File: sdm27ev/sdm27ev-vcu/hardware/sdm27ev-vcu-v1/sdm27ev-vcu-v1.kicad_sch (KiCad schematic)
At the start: 33 parts, among them J1 6437288-1, J2 6437288-1, J4 2201778-1, SW2 SW_Push, SW3 SW_Push, U1 ESP32-P4-Core

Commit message: notes from ev vcu design review 10 3
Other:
- note added: "add sdmmc pullups"
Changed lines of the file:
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@@
+		)
+	)
+	(text "add sdmmc pullups\n"
+		(exclude_from_sim no)
+		(at 96.52 59.436 0)
+		(effects
+			(font
+				(size 1.27 1.27)
+			)
 		)
 	)

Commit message: VCU updates
Updated P4 Symbol
Digital IO protection rework done
Added pending fixes from design review, e.x SDMC pullups
Needs power review - add this to ToDo
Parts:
- removed C1, C2, C3, C5, C6: 100nF, Capacitor_SMD:C_0603_1608Metric, symbol Device:C_Small
- removed C4: 10uF, Capacitor_SMD:C_0603_1608Metric, symbol Device:C_Small
- removed R1, R2: 10k, Resistor_SMD:R_0603_1608Metric, symbol Device:R_Small
- removed SW3: SW_Push, Button_Switch_SMD:SW_SPST_CK_KXT3, symbol Switch:SW_Push
- removed U1: ESP32-P4-Core, symbol SDM_EV:ESP32-P4-Core
- added C10: 10uF, Capacitor_SMD:C_0603_1608Metric, symbol Device:C_Small
- added C11: 100nF, Capacitor_SMD:C_0603_1608Metric, symbol Device:C_Small
- added R80: 10k, Resistor_SMD:R_0603_1608Metric, symbol Device:R_Small
- added RN5: 10k, Resistor_SMD:R_Array_Convex_4x0603, symbol Device:R_Pack04
- added SW1: SW_Push, Button_Switch_SMD:SW_SPST_CK_KXT3, symbol Switch:SW_Push
- added U1: WT0132P4-A1, symbol SDM_EV:WT0132P4-A1
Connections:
- net P4_Reset is gone; now on an unnamed net: R9.1
- net 3.3V: now also R104.2, R87.2; no longer R104.1, R87.1
- net A1: now also U1.74 (GPIO16)
- net A2: now also U1.75 (GPIO17)
- net A3: now also U1.76 (GPIO18)
- net A4: now also U1.77 (GPIO19)
- net A5: now also U1.48 (GPIO49)
- net A6: now also U1.49 (GPIO50)
- net A7: now also U1.50 (GPIO51)
- net A8: now also U1.51 (GPIO52)
- net CAN1_TERM: now also U1.71 (GPIO0)
- net CAN2_TERM: now also U1.72 (GPIO1)
- net CAN3_RX: now also U1.65 (GPIO11)
- net CAN3_TERM: now also U1.55 (GPIO2)
- net CAN3_TX: now also U1.63 (GPIO10)
- net CAN_INT_1: now also U1.61 (GPIO8)
- net CAN_INT_2: now also U1.62 (GPIO9)
- net CAN_SPI2_CS1: now also U1.56 (GPIO3)
- net CAN_SPI2_CS2: now also U1.57 (GPIO4)
- net CAN_SPI2_SCK: now also U1.59 (GPIO6)
- net CAN_SPI2_SDI: now also U1.60 (GPIO7)
- net CAN_SPI2_SDO: now also U1.58 (GPIO5)
- net DI1: now also U1.66 (GPIO12)
- net DI2: now also U1.67 (GPIO13)
- net DI3: now also U1.68 (GPIO14)
- net DI4: now also U1.69 (GPIO15)
- net DO1: now also U1.19 (GPIO24)
- net DO2: now also U1.20 (GPIO25)
- net DO3: now also U1.22 (GPIO26)
- net DO4: now also U1.23 (GPIO27)
- net DO5: now also U1.24 (GPIO28)
- net DO6: now also U1.25 (GPIO29)
- net DO7: now also U1.26 (GPIO30)
- net DO8: now also U1.27 (GPIO31)
- net GND: now also SW2.2, C10.2, C11.2, SW1.1, U1.1 (GND), U1.15 (GND), U1.18 (GND), U1.21 (GND), U1.42 (GND), U1.53 (GND), U1.64 (GND), U1.73 (GND), U1.8 (GND), U1.82 (GND); no longer SW2.1
- net PWR_SCL: now also R87.1; no longer R87.2
- net PWR_SDA: now also R104.1; no longer R104.2
- net SD1-CLK: now also U1.40 (GPIO43)
- net SD1-CMD: now also R80.1, U1.43 (GPIO44)
- net SD1-DAT0: now also RN5.4 (R4.1), U1.36 (GPIO39)
- net SD1-DAT1: now also RN5.3 (R3.1), U1.37 (GPIO40)
- net SD1-DAT2: now also RN5.2 (R2.1), U1.38 (GPIO41)
- net SD1-DAT3: now also RN5.1 (R1.1), U1.39 (GPIO42)
- net StatLED1: now also U1.28 (GPIO32)
- net StatLED2: now also U1.29 (GPIO33)
- net at R51.2: now also U1.16 (USB_DM)
- net at R7.1: now also U1.33 (GPIO36)
- net at R50.1: now also U1.17 (USB_DP)
- net P4_Boot: no longer names the net of R8.1
- net P4_Boot: now also SW2.1, SW1.2, U1.31 (GPIO35), U1.70 (CHIP_PU); no longer SW2.2
- new net 5V: C10.1, C11.1, U1.41 (VCC)
- new net ESP_LDO: R80.2, RN5.5 (R4.2), RN5.6 (R3.2), RN5.7 (R2.2), RN5.8 (R1.2), U1.32 (ESP_LDO_VO4)
- no-connect marks 20 -> 28
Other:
- sheet Digital IO renamed Digital IN-OUT
- sheet Analog ports: added none; removed 5VA, A1_5V, A1_CONN, A2_5V, A2_CONN, A3_5V, A3_CONN, A4_5V, A4_CONN, A5_5V, A5_CONN, A6_5V, A6_CONN, A7_5V, A7_CONN, A8_5V, A8_CONN, A_PWR_INT, SCL, SDA
- sheet CAN ports: added none; removed CAN3_STB, CAN4+, CAN4-, CAN4_RX, CAN4_STB, CAN4_TERM, CAN4_TX, CAN_SPI2_CS2
- sheet Digital IN-OUT ports: added none; removed DI1_CONN, DI2_CONN, DI3_CONN, DI4_CONN, DO1_CONN, DO2_CONN, DO3_CONN, DO4_CONN, DO5_CONN, DO6_CONN, DO7_CONN, DO8_CONN
- note added: "needs power change*"
- note removed: "BULK"
- note removed: "HW SPI*"
- note removed: "add sdmmc pullups"
- moved on the sheet: LED1, LED2, LED3, R106, R107, R108, R14, R15

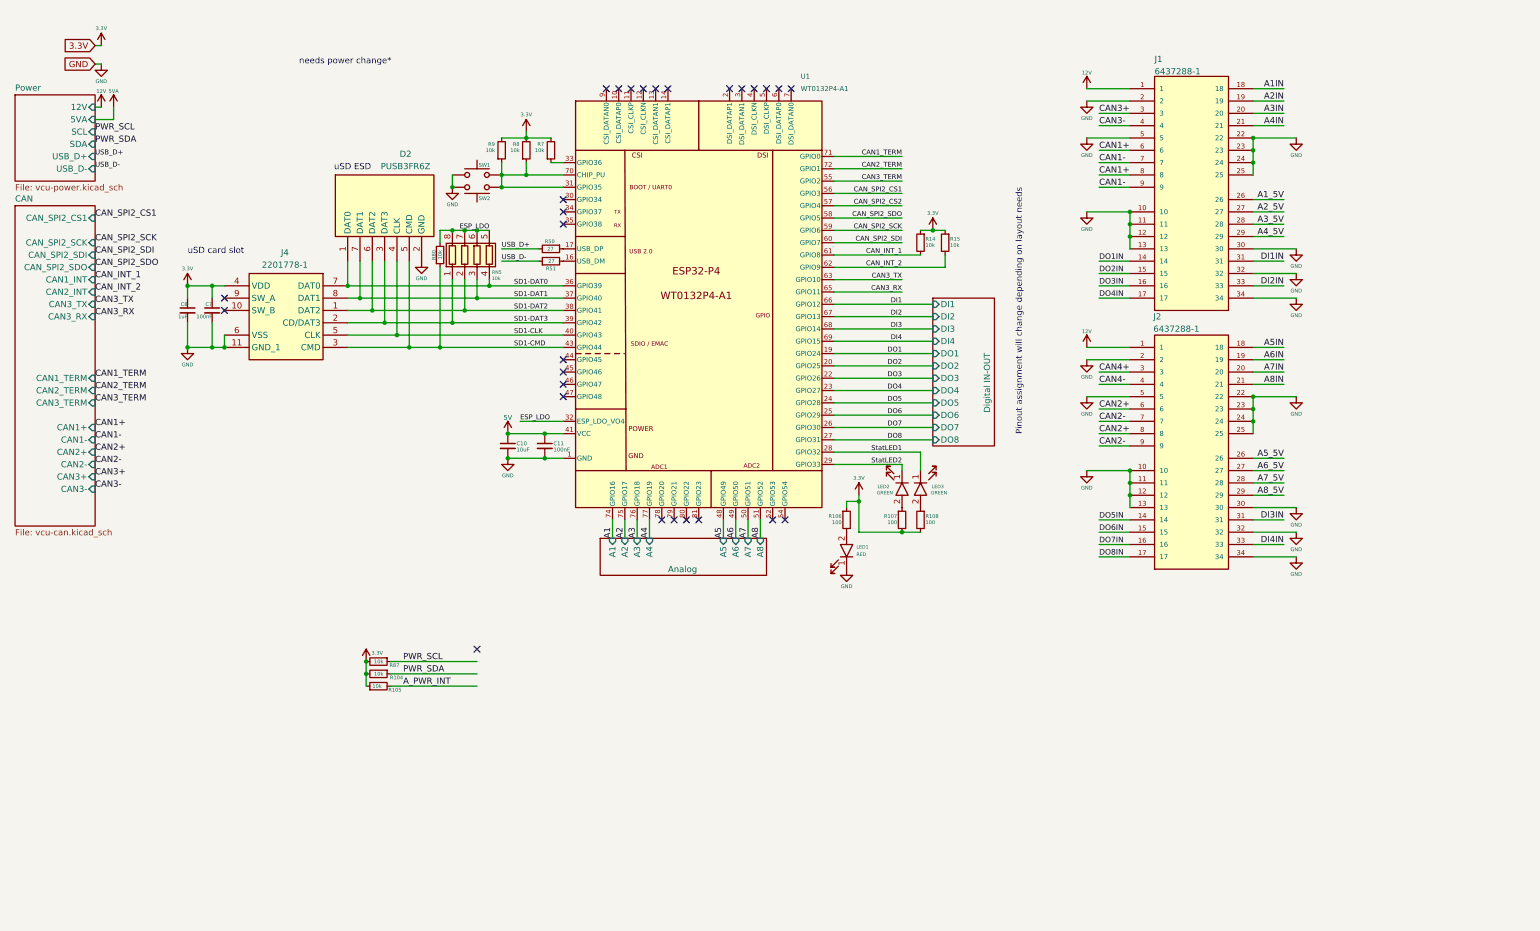
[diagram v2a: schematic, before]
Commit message: VCU sch reorg and power rework
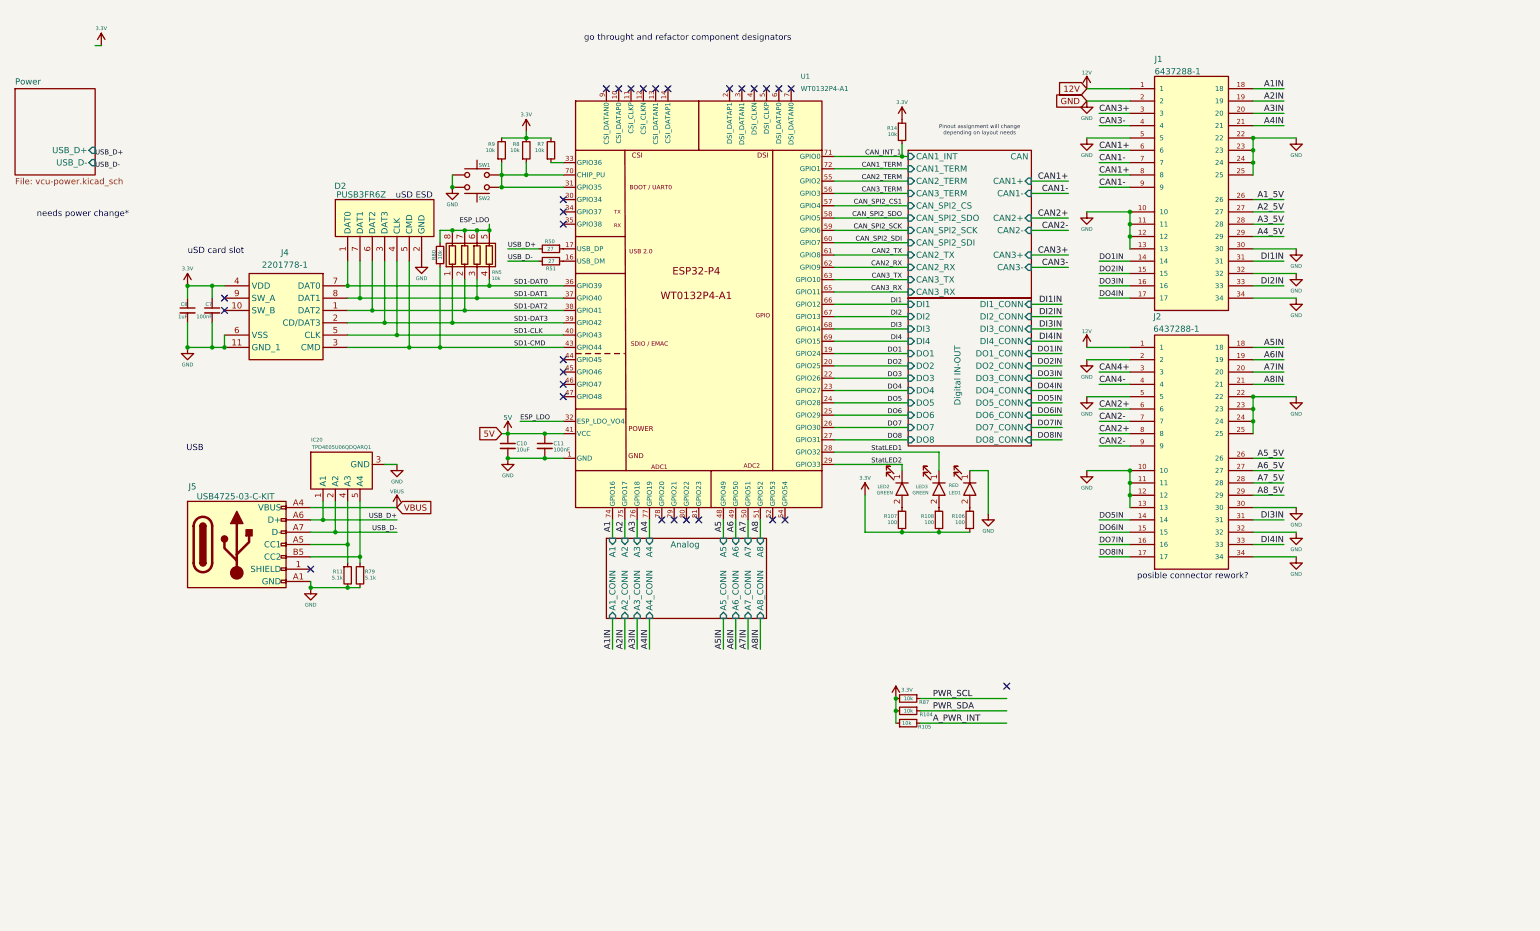
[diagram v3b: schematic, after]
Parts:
- removed R15: 10k, Resistor_SMD:R_0603_1608Metric, symbol Device:R_Small
- added IC20: TPD4E05U06QDQARQ1, DQA(R-PUSON-N10), symbol SDM_EV:TPD4E05U06QDQARQ1
- added J5: USB4725-03-C-KIT, SDM_Misc:GCT_USB4730-GF-A_REVA, symbol SDM_MISC:USB4725-03-C-KIT
- added R11, R79: 5.1k, Resistor_SMD:R_0603_1608Metric, symbol Device:R_Small
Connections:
- net CAN_SPI2_CS2 is gone; now on net CAN_SPI2_CS1: U1.57 (GPIO4)
- net CAN1_TERM: now also U1.72 (GPIO1); no longer U1.71 (GPIO0)
- net CAN2_TERM: now also U1.55 (GPIO2); no longer U1.72 (GPIO1)
- net CAN3_TERM: now also U1.56 (GPIO3); no longer U1.55 (GPIO2)
- net CAN_INT_1: now also U1.71 (GPIO0); no longer U1.61 (GPIO8)
- net CAN_SPI2_CS1: no longer U1.56 (GPIO3)
- net GND: now also IC20.3 (GND), IC20.8 (GND_2), J5.A1 (GND), R11.2, R79.2
- net USB_D+: now also IC20.1 (A1), J5.A6 (D+), J5.B6 (D+)
- net USB_D-: now also IC20.2 (A2), J5.A7 (D-), J5.B7 (D-)
- net CAN_INT_2 renamed CAN2_RX
- new net: IC20.5 (A4), J5.B5 (CC2), R79.1
- new net: IC20.4 (A3), J5.A5 (CC1), R11.1
- new net: IC20.10 (NC_3), IC20.6 (NC_4), IC20.7 (NC_1), IC20.9 (NC_2)
- new net CAN2_TX: U1.61 (GPIO8)
- new net VBUS: J5.A4 (VBUS)
- no-connect marks 28 -> 29
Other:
- sheet Analog ports: added A1_CONN, A2_CONN, A3_CONN, A4_CONN, A5_CONN, A6_CONN, A7_CONN, A8_CONN; removed none
- sheet CAN ports: added CAN2_RX, CAN2_TX, CAN_SPI2_CS; removed CAN2_INT, CAN_SPI2_CS1
- sheet Digital IN-OUT ports: added DI1_CONN, DI2_CONN, DI3_CONN, DI4_CONN, DO1_CONN, DO2_CONN, DO3_CONN, DO4_CONN, DO5_CONN, DO6_CONN, DO7_CONN, DO8_CONN; removed none
- sheet Power ports: added none; removed 12V, 5VA, SCL, SDA
- note added: "USB"
- note added: "go throught and refactor component designators"
- note added: "posible connector rework?"
- moved on the sheet: D2, LED3, R104, R105, R108, R87

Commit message: EV VCU edits, mostly organizational and pre layout/footprint assigned
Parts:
- removed J1, J2: 6437288-1, SDM27 EV VCU:TE_6437288-1, symbol EV VCU:6437288-1
- added J1, J2: 1-776087-1, SDM_EV:17760871, symbol SDM_EV:1-776087-1
- added J3, J6: 6437288-4, SDM_EV:64372884, symbol SDM_EV:6437288-4
- D2: footprint PUSB3FR6Z -> (none)
- IC20: footprint DQA(R-PUSON-N10) -> (none)
- J4: footprint 22017781 -> SDM_EV:22017781
- R50, R51: footprint Resistor_SMD:R_0402_1005Metric -> Resistor_SMD:R_0603_1608Metric
- U1: footprint (none) -> SDM_EV:WT0132P4-A1
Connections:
- net 12V: now also J2.1
- net A1IN: now also J1.1, J3.1
- net A1_5V: now also J1.18, J3.8
- net A2IN: now also J1.2, J3.2
- net A2_5V: now also J1.22, J3.10
- net A3IN: now also J1.3, J3.3
- net A3_5V: now also J2.18
- net A4IN: now also J1.4, J3.4
- net A4_5V: now also J2.22
- net A5IN: now also J2.16
- net A6IN: now also J2.17
- net A7IN: now also J2.20
- net A8IN: now also J2.21
- net CAN1+: now also J2.3
- net CAN1-: now also J2.4
- net CAN2+: now also J1.15
- net CAN2-: now also J1.14
- net CAN2_RX: now also U1.52 (GPIO53); no longer U1.62 (GPIO9)
- net CAN2_TX: now also U1.54 (GPIO54); no longer U1.61 (GPIO8)
- net CAN3+: now also J2.6
- net CAN3-: now also J2.7
- net DI1: now also U1.69 (GPIO15); no longer U1.66 (GPIO12)
- net DI2: now also U1.68 (GPIO14); no longer U1.67 (GPIO13)
- net DI3: now also U1.66 (GPIO12); no longer U1.68 (GPIO14)
- net DI3IN: now also J2.14
- net DI4: now also U1.67 (GPIO13); no longer U1.69 (GPIO15)
- net DI4IN: now also J2.15
- net DO1: now also U1.44 (GPIO45); no longer U1.19 (GPIO24)
- net DO1IN: now also J1.5, J3.12
- net DO2: now also U1.45 (GPIO46); no longer U1.20 (GPIO25)
- net DO2IN: now also J1.6, J3.6
- net DO3: now also U1.46 (GPIO47); no longer U1.22 (GPIO26)
- net DO3IN: now also J1.7, J3.13
- net DO4: now also U1.47 (GPIO48); no longer U1.23 (GPIO27)
- net DO4IN: now also J1.8, J3.7
- net DO5IN: now also J2.9
- net DO6IN: now also J2.10
- net DO7IN: now also J2.11
- net DO8IN: now also J2.12
- net GND: now also J1.13, J1.19, J1.23, J2.13, J2.19, J2.2, J2.23, J2.5, J2.8, J3.11, J3.5, J3.9
- net 5V renamed VCC
- no-connect marks 29 -> 23
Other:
- note added: "in progress"
- note removed: "posible connector rework?"
